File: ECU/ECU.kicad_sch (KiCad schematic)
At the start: 39 parts, among them U1 RP2350A-QFN60, U5 MX25R1635FZUIL0

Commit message: Added Voltage IO sheet, and provisions for the servo, relay, and solenoid control electronics
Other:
- added sheet EMControl (EMControl.kicad_sch)
- added sheet VIOAmplification (VIO.kicad_sch)
- note added: "TO-DO: Voltage I/Os (50% done) UART Comms with other boards Valve control relays/servo"
- note removed: "TO-DO: Voltage I/Os UART Comms with other boards Valve control relays/servo"

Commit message: finished ECU
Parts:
- added J3: USB_C_Receptacle_USB2.0_16P, Connector_USB:USB_C_Receptacle_HRO_TYPE-C-31-M-12, symbol Connector:USB_C_Receptacle_USB2.0_16P
- added R26, R27: 5.1k, Resistor_SMD:R_0805_2012Metric_Pad1.20x1.40mm_HandSolder, symbol Device:R
- added R28, R29: 27, Resistor_SMD:R_0805_2012Metric_Pad1.20x1.40mm_HandSolder, symbol Device:R
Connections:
- net +1V1: now also L1.2, U1.48 (VREG_LX)
- net CS1: now also U1.28 (GPIO17)
- net CS2: now also U1.29 (GPIO18)
- net GND: now also J3.A1 (GND), J3.A12 (GND), J3.B1 (GND), J3.B12 (GND), R26.2, R27.2
- net RX: now also U1.31 (GPIO19)
- net TX: now also U1.32 (GPIO20)
- net Outputs (page 3)/Servo0: now reaches U1.17 (GPIO13)
- net Outputs (page 3)/Servo1: now reaches U1.18 (GPIO14)
- net Outputs (page 3)/Servo2: now reaches U1.19 (GPIO15)
- net Outputs (page 3)/Servo3: now reaches U1.27 (GPIO16)
- net at U1.51 (USB_DM): now also R28.2
- net at U1.52 (USB_DP): now also R29.2
- removed net AIN0: R10.2, R14.1, R18.2, R2.1, R22.1, R6.2
- removed net AIN1: R11.2, R16.1, R19.2, R24.1, R3.1, R7.2
- removed net AIN2: R12.2, R15.2, R20.2, R23.2, R5.2, R8.2
- removed net AIN3: R13.2, R17.1, R21.2, R25.1, R4.1, R9.2
- new net: J3.A5 (CC1), R27.1
- new net: J3.A6 (D+), J3.B6 (D+), R29.1
- new net: J3.A7 (D-), J3.B7 (D-), R28.1
- new net: J3.B5 (CC2), R26.1
- new net CIN0: R2.1, R6.2
- new net CIN1: R3.1, R7.2
- new net CIN10: R20.2, R23.2
- new net CIN11: R21.2, R25.1
- new net CIN2: R5.2, R8.2
- new net CIN3: R4.1, R9.2
- new net CIN4: R10.2, R14.1
- new net CIN5: R11.2, R16.1
- new net CIN6: R12.2, R15.2
- new net CIN7: R13.2, R17.1
- new net CIN8: R18.2, R22.1
- new net CIN9: R19.2, R24.1
- new net USB_VBUS: J3.A4 (VBUS), J3.A9 (VBUS), J3.B4 (VBUS), J3.B9 (VBUS)
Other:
- sheet EMControl renamed Outputs (page 3)
- sheet Outputs (page 3) ports: added 5V, CIN0, CIN1, CIN10, CIN11, CIN2, CIN3, CIN4, CIN5, CIN6, CIN7, CIN8, CIN9, MCU3V3, MCUGND, RX, Servo0, Servo1, Servo2, Servo3, Servo5V, ServoGND, TX, VIN0, VIN1, VIN2, VIN3, VIN4, VIN5, VIN6, VIN7; removed none
- sheet VIOAmplification ports: added RST; removed CLKIN
- note added: "TO-DO: Voltage I/Os (50% done) tick UART Comms with other boards Valve control relays/servo tick"
- note removed: "TO-DO: Voltage I/Os (50% done) UART Comms with other boards Valve control relays/servo"

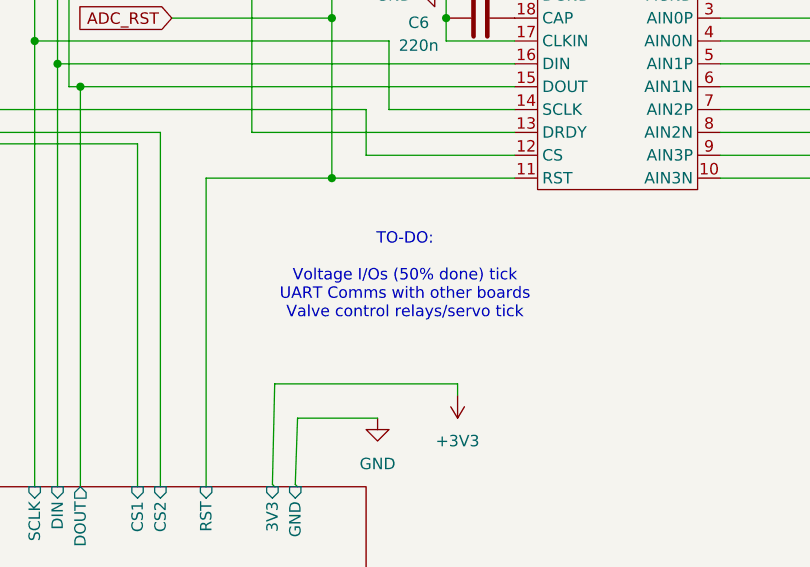
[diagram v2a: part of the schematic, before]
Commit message: VIO added
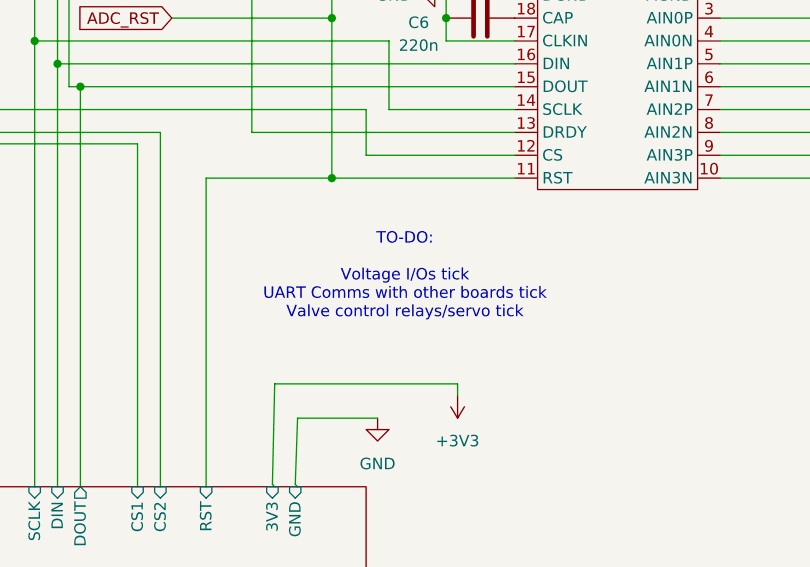
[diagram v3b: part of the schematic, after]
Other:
- note added: "TO-DO: Voltage I/Os tick UART Comms with other boards tick Valve control relays/servo tick"
- note removed: "TO-DO: Voltage I/Os (50% done) tick UART Comms with other boards Valve control relays/servo tick"
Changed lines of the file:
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@@
 		)
 	)
-	(text "TO-DO:\n\nVoltage I/Os (50% done) tick\nUART Comms with other boards\nValve control relays/servo tick\n\n"
+	(text "TO-DO:\n\nVoltage I/Os tick\nUART Comms with other boards tick\nValve control relays/servo tick\n\n"
 		(exclude_from_sim no)
 		(at 170.688 136.398 0)

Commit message: small changes
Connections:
- net Outputs (page 3)/VIO2: now reaches U1.34 (GPIO22)
- net Outputs (page 3)/VIO1: now reaches U1.35 (GPIO23)
- net Outputs (page 3)/VIO0: now reaches U1.36 (GPIO24)
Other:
- sheet Outputs (page 3) ports: added VIO0, VIO1, VIO2, VIO3; removed none
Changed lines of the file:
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@@
 	(wire
 		(pts
+			(xy 17.78 166.37) (xy 16.51 166.37)
+		)
+		(stroke
+			(width 0)
+			(type default)
+		)
+	)
+	(wire
+		(pts
 			(xy 104.14 181.61) (xy 104.14 194.31)
 		)
@@
 	(wire
 		(pts
+			(xy 17.526 163.83) (xy 17.526 128.27)
+		)
+		(stroke
+			(width 0)
+			(type default)
+		)
+	)
+	(wire
+		(pts
 			(xy 234.95 121.92) (xy 246.38 121.92)
 		)
@@
 	(wire
 		(pts
+			(xy 60.96 120.65) (xy 60.96 123.19)
+		)
+		(stroke
+			(width 0)
+			(type default)
+		)
+	)
+	(wire
+		(pts
 			(xy 237.49 116.84) (xy 271.78 116.84)
 		)
@@
 	(wire
 		(pts
+			(xy 110.49 127) (xy 110.49 125.73)
+		)
+		(stroke
+			(width 0)
+			(type default)
+		)
+	)
+	(wire
+		(pts
 			(xy 143.51 99.06) (xy 153.67 99.06)
 		)
@@
 	(wire
 		(pts
+			(xy 15.24 120.65) (xy 60.96 120.65)
+		)
+		(stroke
+			(width 0)
+			(type default)
+		)
+	)
+	(wire
+		(pts
 			(xy 132.08 81.28) (xy 132.08 111.76)
 		)
@@
 	(wire
 		(pts
+			(xy 16.51 127) (xy 110.49 127)
+		)
+		(stroke
+			(width 0)
+			(type default)
+		)
+	)
+	(wire
+		(pts
 			(xy 111.76 57.15) (xy 111.76 48.26)
 		)
@@
 	(wire
 		(pts
+			(xy 17.78 168.91) (xy 15.24 168.91)
+		)
+		(stroke
+			(width 0)
+			(type default)
+		)
+	)
+	(wire
+		(pts
 			(xy 26.67 80.01) (xy 27.94 80.01)
 		)
@@
 	(wire
 		(pts
+			(xy 16.51 166.37) (xy 16.51 127)
+		)
+		(stroke
+			(width 0)
+			(type default)
+		)
+	)
+	(wire
+		(pts
 			(xy 175.26 109.22) (xy 175.26 106.68)
 		)
@@
 	(wire
 		(pts
+			(xy 17.78 163.83) (xy 17.526 163.83)
+		)
+		(stroke
+			(width 0)
+			(type default)
+		)
+	)
+	(wire
+		(pts
 			(xy 129.54 45.72) (xy 171.45 45.72)
 		)
@@
 	(wire
 		(pts
+			(xy 15.24 168.91) (xy 15.24 120.65)
+		)
+		(stroke
+			(width 0)
+			(type default)
+		)
+	)
+	(wire
+		(pts
 			(xy 133.35 74.93) (xy 133.35 83.82)
 		)
@@
 	(wire
 		(pts
+			(xy 60.96 123.19) (xy 110.49 123.19)
+		)
+		(stroke
+			(width 0)
+			(type default)
+		)
+	)
+	(wire
+		(pts
 			(xy 171.45 31.75) (xy 177.8 31.75)
 		)
@@
 	(wire
 		(pts
+			(xy 17.526 128.27) (xy 110.49 128.27)
+		)
+		(stroke
+			(width 0)
+			(type default)
+		)
+	)
+	(wire
+		(pts
 			(xy 227.33 48.26) (xy 205.74 48.26)
 		)
@@
 			)
 		)
+		(pin "VIO0" input
+			(at 17.78 163.83 180)
+			(effects
+				(font
+					(size 1.27 1.27)
+				)
+				(justify left)
+			)
+		)
+		(pin "VIO1" input
+			(at 17.78 166.37 180)
+			(effects
+				(font
+					(size 1.27 1.27)
+				)
+				(justify left)
+			)
+		)
+		(pin "VIO2" input
+			(at 17.78 168.91 180)
+			(effects
+				(font
+					(size 1.27 1.27)
+				)
+				(justify left)
+			)
+		)
+		(pin "VIO3" input
+			(at 17.78 171.45 180)
+			(effects
+				(font
+					(size 1.27 1.27)
+				)
+				(justify left)
+			)
+		)
